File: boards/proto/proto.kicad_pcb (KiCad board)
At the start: 2 copper layers, 100 x 100 mm, 9 parts, among them J1 XBUS_02, J2 PIA_INT, J3 VIA_INT, J4 ACIA_INT

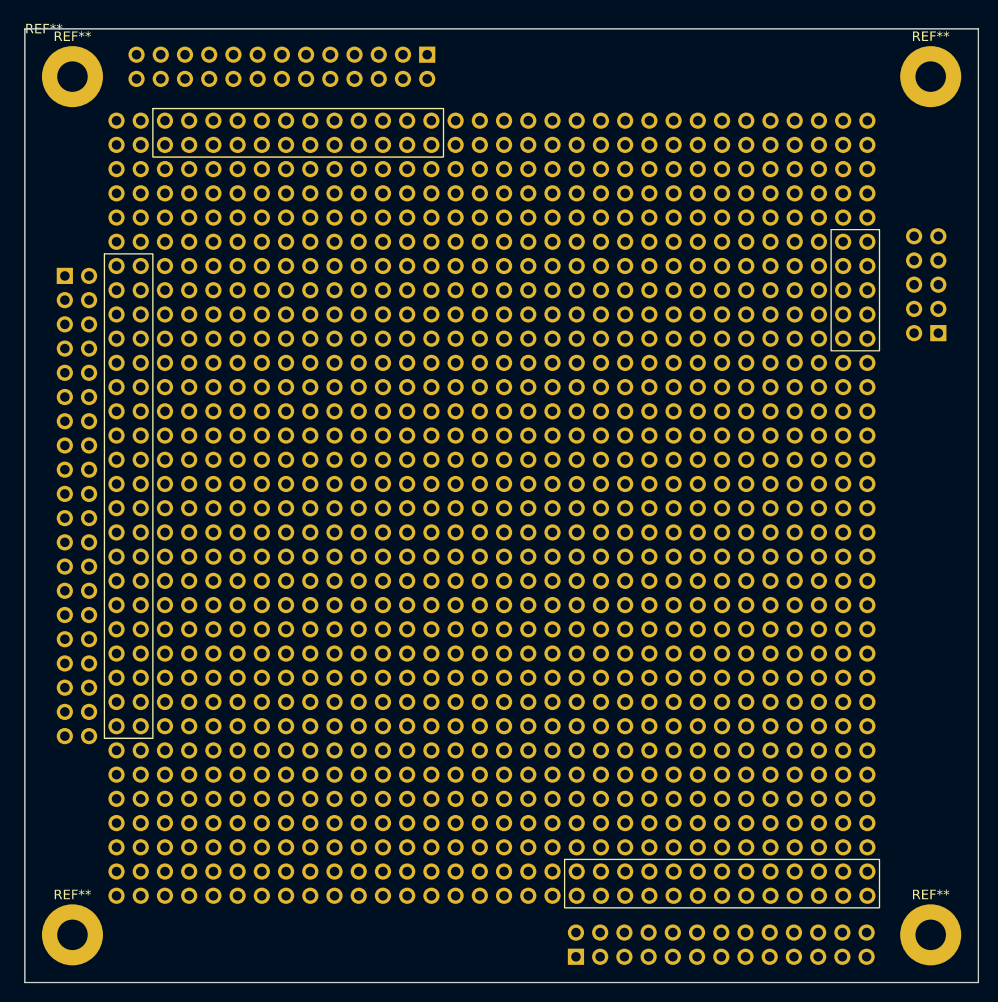
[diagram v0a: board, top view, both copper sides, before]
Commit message: Create symbol for prototype area to break out connectors.
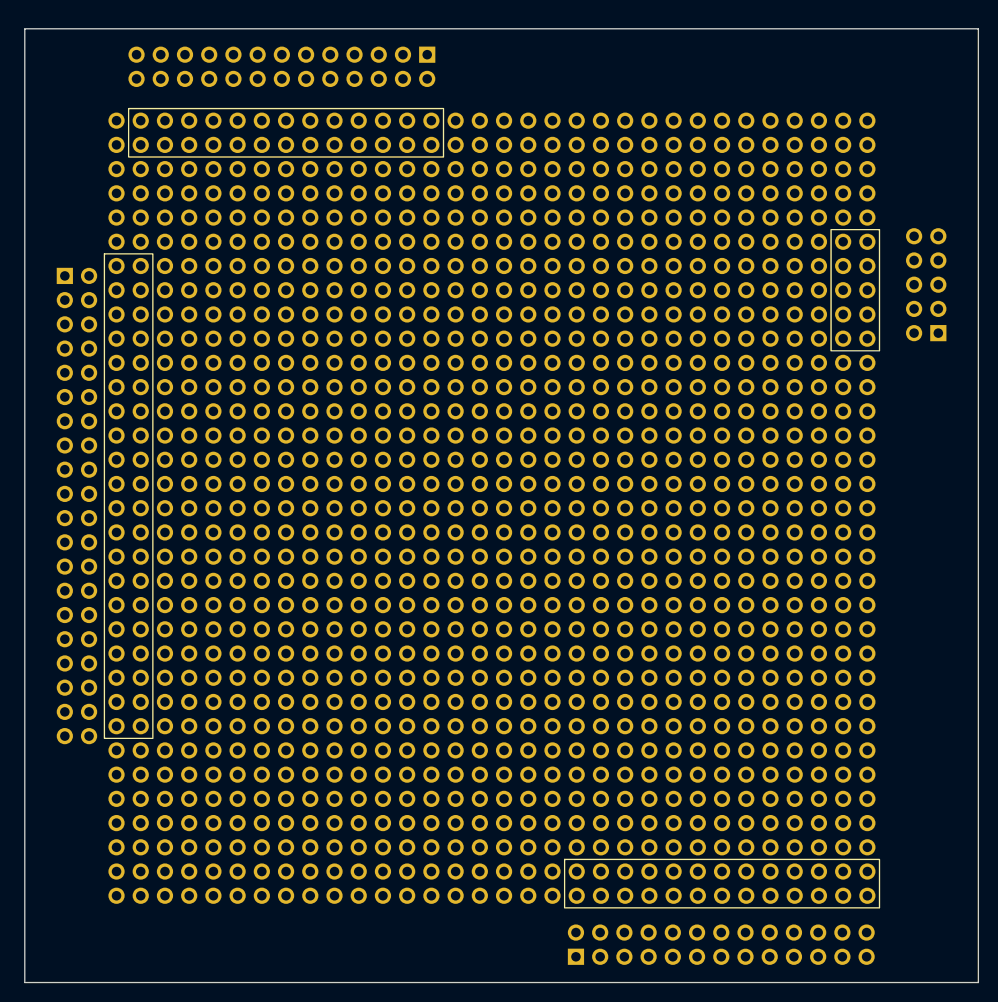
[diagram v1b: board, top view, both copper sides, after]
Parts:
- removed REF** (x4): MountingHole_3.2mm_M3_Pad, MountingHole:MountingHole_3.2mm_M3_Pad
- REF5: renamed from REF**; value Prototype Area -> PROTO
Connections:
- REF5 pad 10: (no net) -> VIA_PA4
- REF5 pad 1012: (no net) -> GND
- REF5 pad 1013: (no net) -> PIA_CA2
- REF5 pad 1014: (no net) -> PIA_PA1
- REF5 pad 1015: (no net) -> PIA_PA3
- REF5 pad 1016: (no net) -> PIA_PA5
- REF5 pad 1017: (no net) -> PIA_PA7
- REF5 pad 1018: (no net) -> GND
- REF5 pad 1019: (no net) -> PIA_CB2
- REF5 pad 1020: (no net) -> PIA_PB1
- REF5 pad 1021: (no net) -> PIA_PB3
- REF5 pad 1022: (no net) -> PIA_PB5
- REF5 pad 1023: (no net) -> PIA_PB7
- REF5 pad 1024: (no net) -> +5V
- REF5 pad 1044: (no net) -> +5V
- REF5 pad 1045: (no net) -> PIA_CA1
- REF5 pad 1046: (no net) -> PIA_PA0
- REF5 pad 1047: (no net) -> PIA_PA2
- REF5 pad 1048: (no net) -> PIA_PA4
- REF5 pad 1049: (no net) -> PIA_PA6
- REF5 pad 1050: (no net) -> GND
- REF5 pad 1051: (no net) -> PIA_CB1
- REF5 pad 1052: (no net) -> PIA_PB0
- REF5 pad 1053: (no net) -> PIA_PB2
- REF5 pad 1054: (no net) -> PIA_PB4
- REF5 pad 1055: (no net) -> PIA_PB6
- REF5 pad 1056: (no net) -> GND
- REF5 pad 11: (no net) -> VIA_PA2
- REF5 pad 12: (no net) -> VIA_PA0
- REF5 pad 13: (no net) -> VIA_CA1
- REF5 pad 14: (no net) -> +5V
- REF5 pad 191: (no net) -> ACIA_RXC
- REF5 pad 192: (no net) -> ACIA_CTSB
- REF5 pad 193: (no net) -> +5V
- REF5 pad 194: (no net) -> GND
- REF5 pad 2: (no net) -> GND
- REF5 pad 223: (no net) -> ACIA_DCDB
- REF5 pad 224: (no net) -> ACIA_TXD
- REF5 pad 225: (no net) -> D0
- REF5 pad 226: (no net) -> D1
- REF5 pad 255: (no net) -> ACIA_DSRB
- REF5 pad 256: (no net) -> ACIA_RXD
- REF5 pad 257: (no net) -> D2
- REF5 pad 258: (no net) -> D3
- REF5 pad 287: (no net) -> ACIA_DTRB
- REF5 pad 288: (no net) -> ACIA_RTSB
- REF5 pad 289: (no net) -> D4
- REF5 pad 290: (no net) -> D5
- REF5 pad 3: (no net) -> VIA_PB6
- REF5 pad 319: (no net) -> GND
- REF5 pad 320: (no net) -> +5V
- REF5 pad 321: (no net) -> D6
- REF5 pad 322: (no net) -> D7
- REF5 pad 34: (no net) -> +5V
- REF5 pad 35: (no net) -> VIA_PB7
- REF5 pad 353: (no net) -> A0
- REF5 pad 354: (no net) -> A1
- REF5 pad 36: (no net) -> VIA_PB5
- REF5 pad 37: (no net) -> VIA_PB3
- REF5 pad 38: (no net) -> VIA_PB1
- REF5 pad 385: (no net) -> A2
- REF5 pad 386: (no net) -> A3
- REF5 pad 39: (no net) -> VIA_CB2
- REF5 pad 4: (no net) -> VIA_PB4
- REF5 pad 40: (no net) -> GND
- REF5 pad 41: (no net) -> VIA_PA7
- REF5 pad 417: (no net) -> A4
- REF5 pad 418: (no net) -> A5
- REF5 pad 42: (no net) -> VIA_PA5
- REF5 pad 43: (no net) -> VIA_PA3
- REF5 pad 44: (no net) -> VIA_PA1
- REF5 pad 449: (no net) -> A6
- REF5 pad 45: (no net) -> VIA_CA2
- REF5 pad 450: (no net) -> A7
- REF5 pad 46: (no net) -> GND
- REF5 pad 481: (no net) -> A8
- REF5 pad 482: (no net) -> A9
- REF5 pad 5: (no net) -> VIA_PB2
- REF5 pad 513: (no net) -> A10
- REF5 pad 514: (no net) -> A11
- REF5 pad 545: (no net) -> A12
- REF5 pad 546: (no net) -> A13
- REF5 pad 577: (no net) -> A14
- REF5 pad 578: (no net) -> A15
- REF5 pad 6: (no net) -> VIA_PB0
- REF5 pad 609: (no net) -> XCSB0
- REF5 pad 610: (no net) -> XCSB1
- REF5 pad 641: (no net) -> XCSB2
- REF5 pad 642: (no net) -> VPB
- REF5 pad 673: (no net) -> IRQB
- REF5 pad 674: (no net) -> NMIB
- REF5 pad 7: (no net) -> VIA_CB1
- REF5 pad 705: (no net) -> RESB
- REF5 pad 706: (no net) -> MLB
- REF5 pad 737: (no net) -> SYNC
- REF5 pad 738: (no net) -> BE
- REF5 pad 769: (no net) -> RWB
- REF5 pad 770: (no net) -> PHI2
- REF5 pad 8: (no net) -> GND
- REF5 pad 801: (no net) -> GND
- REF5 pad 802: (no net) -> +5V
- REF5 pad 9: (no net) -> VIA_PA6

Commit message: Route header breakouts except power.
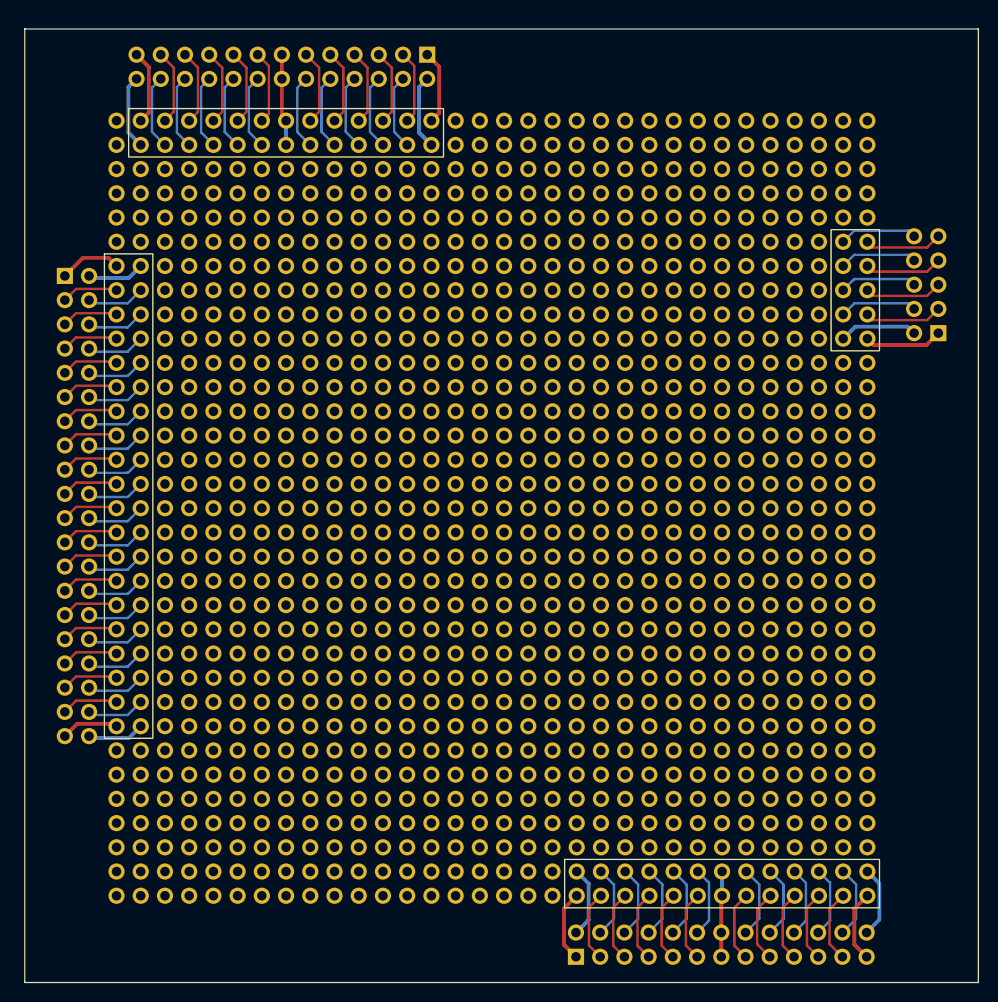
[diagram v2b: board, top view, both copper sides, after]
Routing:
- net GND: track 0.00 -> 69.5 mm
- net +5V: track 0.00 -> 51.3 mm
- net ACIA_CTSB: track 0.00 -> 8.17 mm
- net ACIA_TXD: track 0.00 -> 8.17 mm
- net ACIA_RXD: track 0.00 -> 8.17 mm
- net ACIA_RXC: track 0.00 -> 8.17 mm
- net ACIA_RTSB: track 0.00 -> 8.17 mm
- net ACIA_DTRB: track 0.00 -> 8.17 mm
- net ACIA_DSRB: track 0.00 -> 8.17 mm
- net ACIA_DCDB: track 0.00 -> 8.17 mm
- net VIA_PB7: track 0.00 -> 7.87 mm
- net VIA_PB4: track 0.00 -> 7.87 mm
- net VIA_PA5: track 0.00 -> 7.87 mm
- net VIA_PA1: track 0.00 -> 7.87 mm
- net VIA_PB0: track 0.00 -> 7.87 mm
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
